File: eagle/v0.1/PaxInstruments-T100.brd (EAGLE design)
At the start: 47.9 x 17.1 mm, 28 parts, among them J1 AVR_SPI_PRG_6PTH, U1 Attiny85

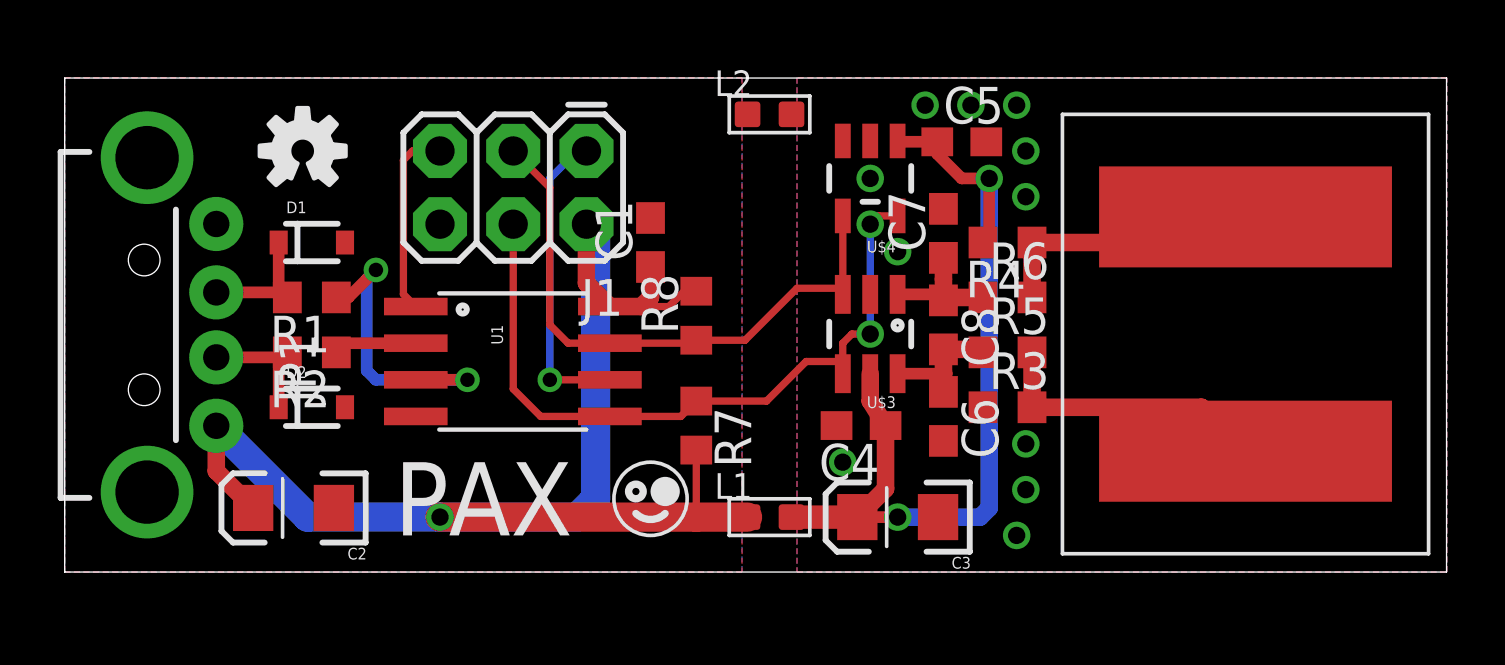
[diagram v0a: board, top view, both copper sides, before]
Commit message: ISP connector is modified.
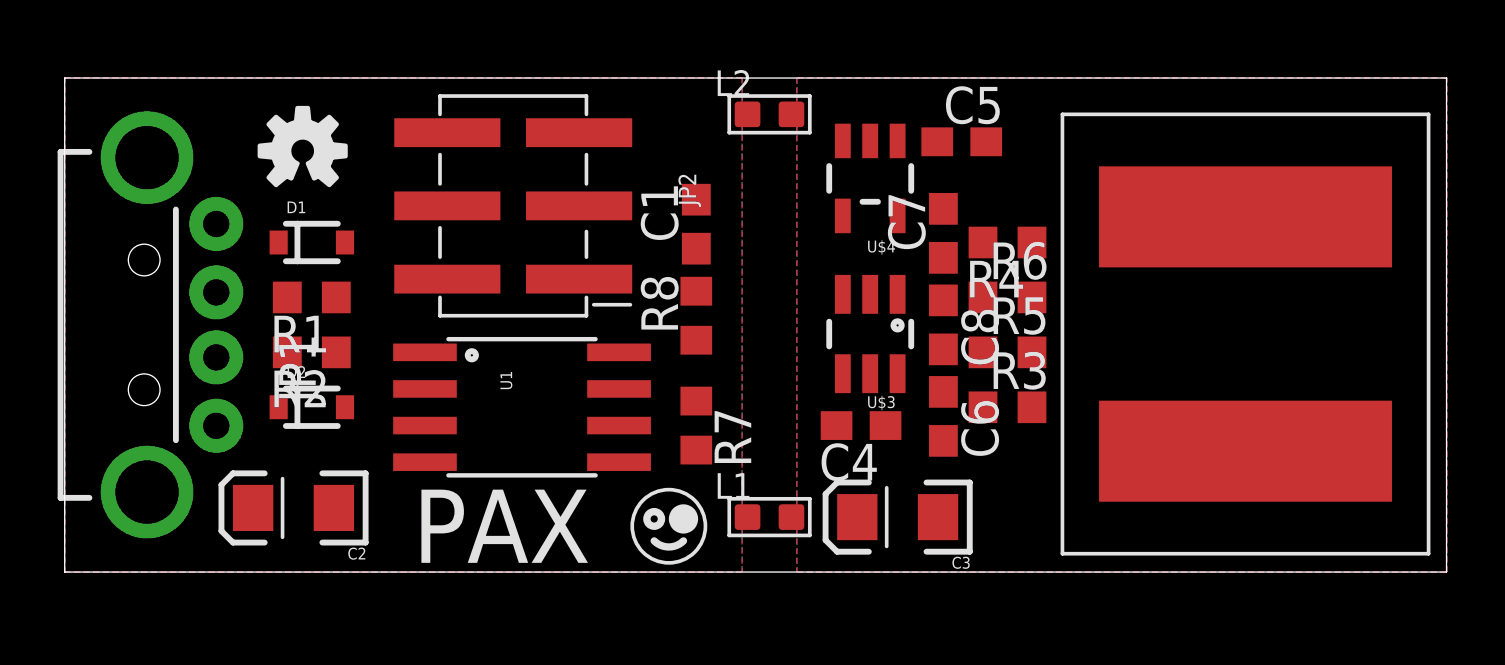
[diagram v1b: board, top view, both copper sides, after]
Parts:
- removed J1: AVR_SPI_PRG_6PTH, SparkFun-Connectors:2X3
- added JP2: (no value), SparkFun-Connectors:2X3_SMT_POSTS
- moved C1 1.71 mm to (21.9, 12.1)
- moved U1 1.62 mm to (15.9, 5.71)
- moved U$1 1.14 mm to (12.1, 0.32)
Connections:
- net /RST: now also JP2.5; no longer J1.5
- net GND: now also JP2.6; no longer J1.6
- net SCL: now also JP2.3; no longer J1.3
- net SDA: now also JP2.4; no longer J1.4
- net SPARE: now also JP2.1; no longer J1.1
- net USB_5V: now also JP2.2; no longer J1.2
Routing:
- net USB_5V: track 48.7 -> 0.00 mm, vias 1 -> 0
- net A_5V: track 30.2 -> 0.00 mm, vias 2 -> 0
- net SDA: track 25.7 -> 0.00 mm, vias 2 -> 0
- net SCL: track 20.6 -> 0.00 mm
- net D+: track 10.8 -> 0.00 mm, vias 2 -> 0
- net SPARE: track 10.7 -> 0.00 mm, vias 1 -> 0
- net N$3: track 9.94 -> 0.00 mm
- net N$4: track 9.68 -> 0.00 mm
- net /RST: track 6.66 -> 0.00 mm
- net TC-: track 5.44 -> 0.00 mm
- net TC+: track 5.13 -> 0.00 mm
- net N$2: track 4.67 -> 0.00 mm
- net N$1: track 4.57 -> 0.00 mm
- net D-: track 2.89 -> 0.00 mm

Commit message: Layout changes with thermal cutout
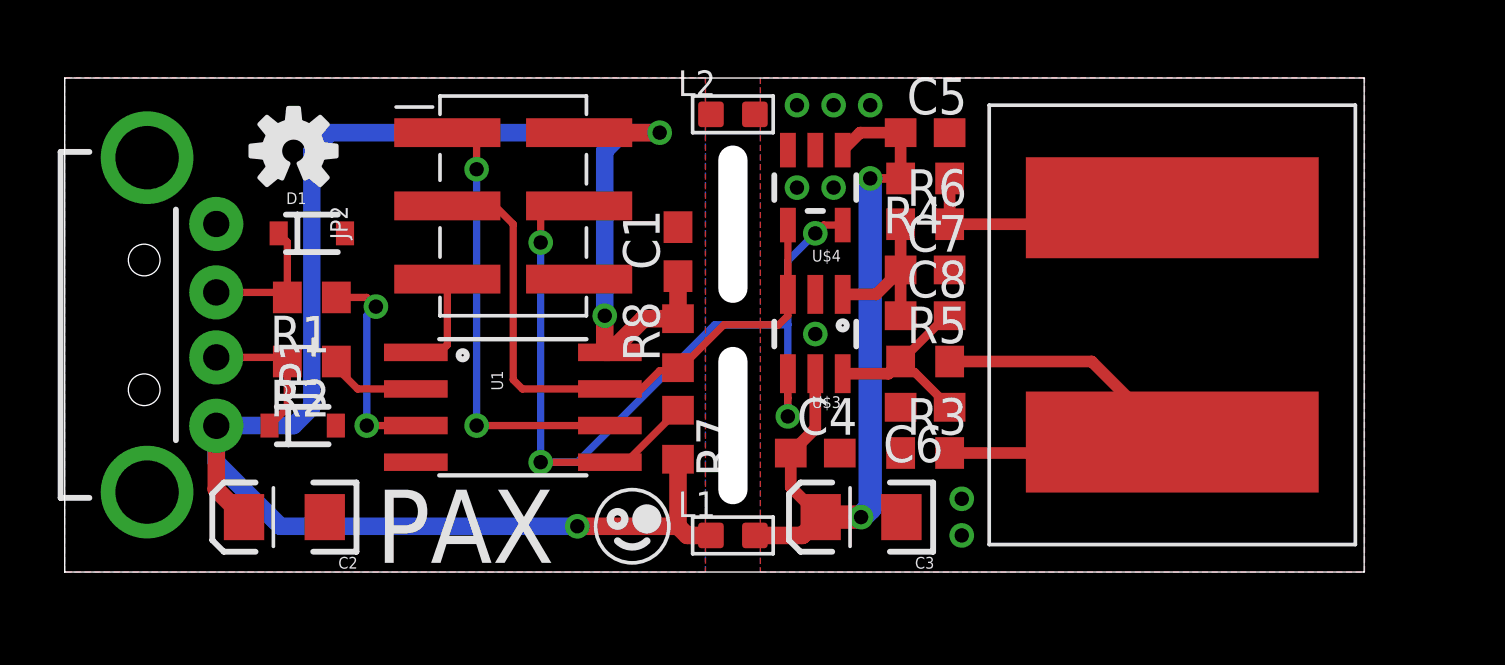
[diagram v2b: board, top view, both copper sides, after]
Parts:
- moved R6 3.82 mm to (29.8, 12.1)
- moved R4 3.62 mm to (29.8, 13.7)
- moved R3 3.27 mm to (29.8, 4.13)
- moved R5 2.88 mm to (29.8, 7.30)
- moved U$2 2.56 mm to (38.4, 8.57)
- moved U$4 1.93 mm to (26.0, 13.3)
- moved U$3 1.91 mm to (26.0, 8.26)
- moved C4 1.85 mm to (26.0, 4.13), turned to 0 degrees
- moved L1 1.42 mm to (23.2, 1.27)
- moved C7 1.42 mm to (29.8, 10.5), turned to 0 degrees
- moved C5 1.31 mm to (29.8, 15.2)
- moved L2 1.27 mm to (23.2, 15.9)
- moved C3 1.27 mm to (27.6, 1.91)
- moved U$1 1.27 mm to (10.8, 0.32)
- moved R8 1.14 mm to (21.3, 7.94)
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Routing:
- net USB_5V: track 0.00 -> 65.3 mm, vias 0 -> 3
- net SDA: track 0.00 -> 35.4 mm, vias 0 -> 4
- net A_5V: track 0.00 -> 26.5 mm, vias 0 -> 2
- net SCL: track 0.00 -> 21.8 mm
- net N$3: track 0.00 -> 16.8 mm
- net SPARE: track 0.00 -> 15.8 mm, vias 0 -> 2
- net N$4: track 0.00 -> 10.4 mm
- net D+: track 0.00 -> 7.46 mm, vias 0 -> 2
- net TC-: track 0.00 -> 7.12 mm
- net TC+: track 0.00 -> 5.54 mm
- net N$1: track 0.00 -> 5.00 mm
- net N$2: track 0.00 -> 4.88 mm
- net /RST: track 0.00 -> 3.48 mm
- net D-: track 0.00 -> 3.28 mm
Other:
- board size 47.9 x 17.1 mm -> 45.1 x 17.1 mm

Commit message: Fixed clearance issues, added round corners and version number to the layout
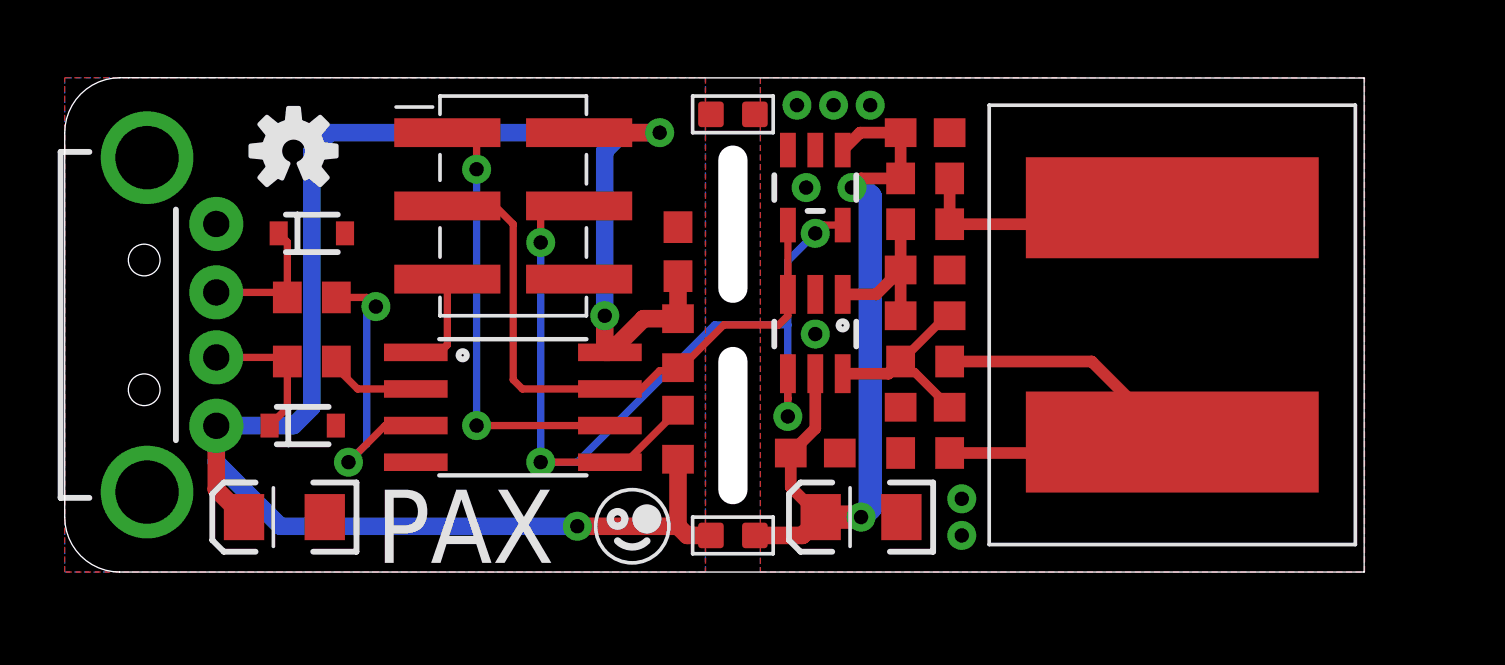
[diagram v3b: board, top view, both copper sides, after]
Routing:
- net D+: track 7.46 -> 10.2 mm
- net A_5V: track 26.5 -> 27.4 mm
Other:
- outline, holes or cut-outs redrawn
- board text added: "Pax Instruments T-100 [v0.1] November 2014"
